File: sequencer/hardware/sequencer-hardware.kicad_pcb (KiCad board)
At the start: 4 copper layers, 100.6 x 151.4 mm, 116 parts, among them J1 Barrel Jack, J10 JST_4-pin_male, J11 Conn_01x03, J12 Conn_01x03, J13 Conn_01x03, J14 Conn_01x03, J15 JST_4-pin_male, J16 JST_4-pin_male, J17 Conn_01x03, J2 40Pin 0.1"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

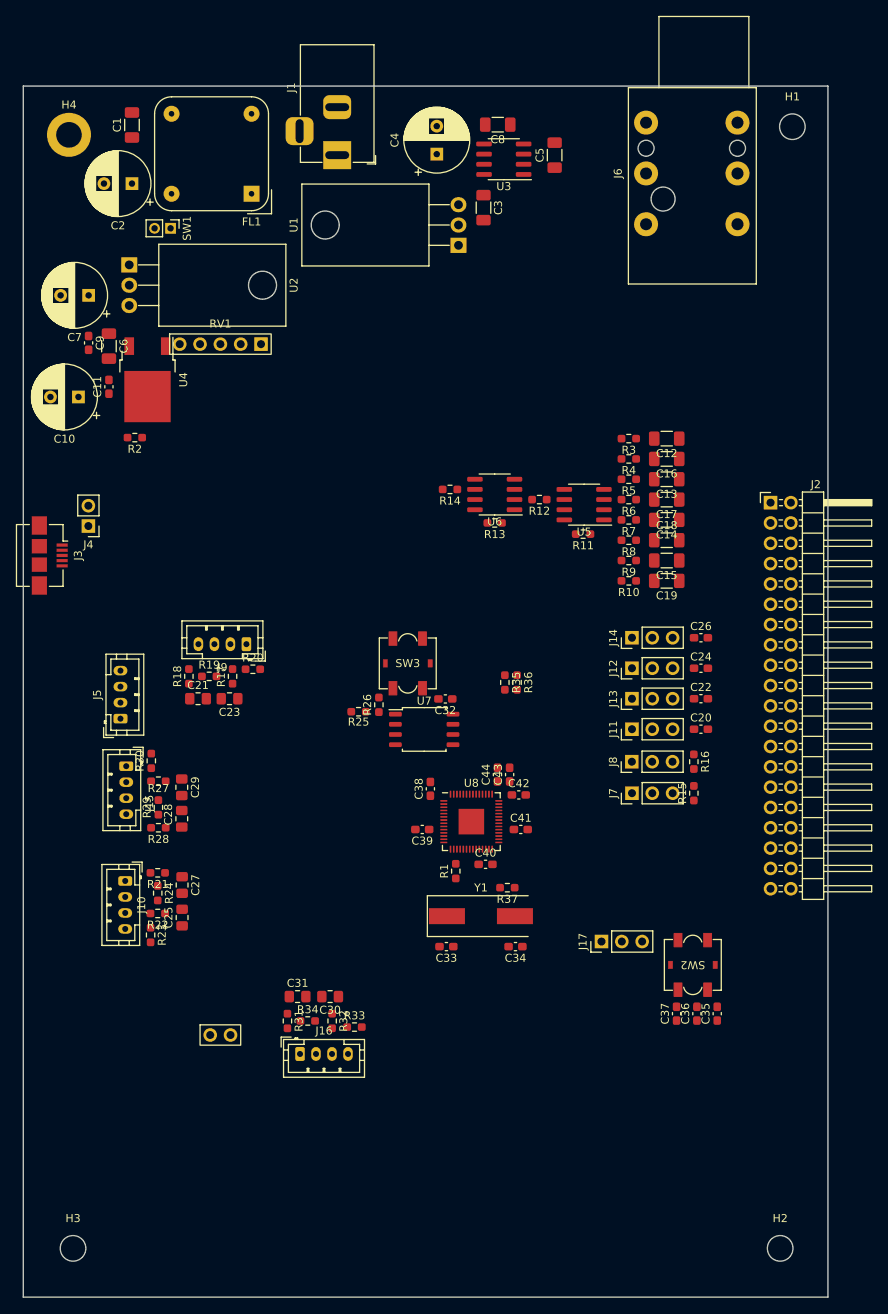
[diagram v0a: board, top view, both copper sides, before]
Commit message: Add ground planes
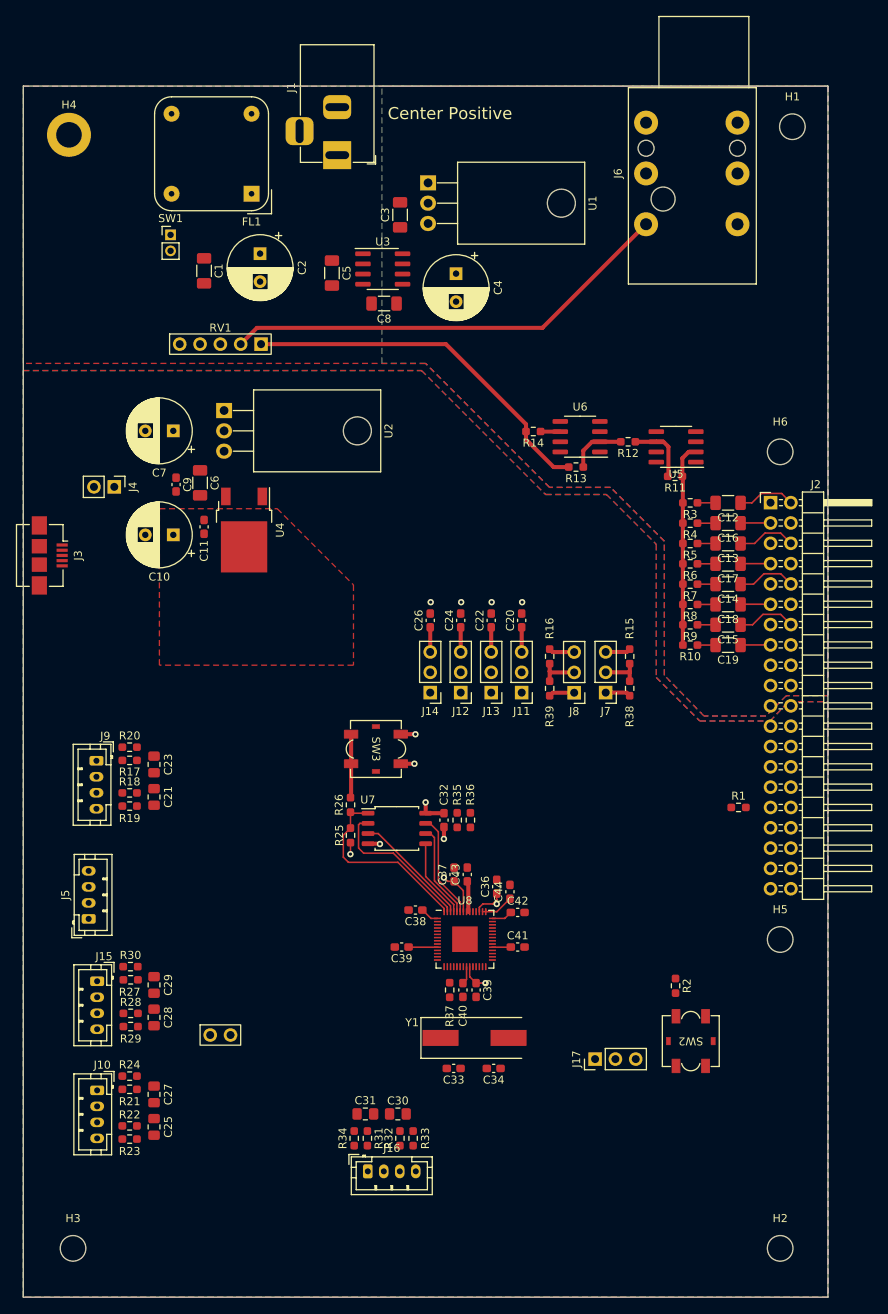
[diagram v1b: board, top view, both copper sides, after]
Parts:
- added H5: MountingHole, MountingHole:MountingHole_3.2mm_M3_ISO14580, F.Cu at (120.0, 132.1)
- added H6: MountingHole, MountingHole:MountingHole_3.2mm_M3_ISO14580, F.Cu at (120.0, 71.1)
- added R38: 10k, Resistor_SMD:R_0603_1608Metric_Pad0.98x0.95mm_HandSolder, F.Cu at (101.2, 100.7)
- added R39: 10k, Resistor_SMD:R_0603_1608Metric_Pad0.98x0.95mm_HandSolder, F.Cu at (91.2, 100.7)
- moved R2 96.2 mm to (106.9, 137.9), turned to -90 degrees
- moved R1 36.2 mm to (114.8, 115.6), turned to 0 degrees
- moved C26 33.9 mm to (76.3, 92.2), turned to 90 degrees
- moved C37 32.8 mm to (79.2, 124.0)
- moved C5 31.5 mm to (64.0, 48.8), turned to -90 degrees
- moved C24 30.6 mm to (80.1, 92.2), turned to 90 degrees
- moved C35 30.3 mm to (82.0, 138.4), turned to -90 degrees
- moved C36 29.6 mm to (84.6, 125.5)
- moved C22 28.0 mm to (83.9, 92.2), turned to 90 degrees
- moved R29 27.6 mm to (38.8, 143.0), turned to 0 degrees
- moved R21 27.3 mm to (38.7, 150.8)
- moved J15 27.1 mm to (34.6, 137.3)
- moved R22 26.8 mm to (38.7, 155.4)
- moved C8 26.5 mm to (70.5, 52.6), turned to 0 degrees
- moved C27 26.4 mm to (41.7, 151.4)
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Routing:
- net Net-(J6-PadT): track 0.00 -> 56.9 mm
- net Net-(R13-Pad2): track 0.00 -> 45.9 mm
- net +3V3: track 0.00 -> 45.2 mm, vias 0 -> 2
- net Net-(R10-Pad2): track 0.00 -> 25.4 mm
- net /D.R.U.M. Sequencer Digital/FCSB: track 0.00 -> 23.9 mm
- net /D.R.U.M. Sequencer Digital/FD1: track 0.00 -> 18.9 mm
- net /D.R.U.M. Sequencer Digital/FD2: track 0.00 -> 14.8 mm
- net +1V1: track 0.00 -> 14.2 mm, vias 0 -> 3
- net /D.R.U.M. Sequencer Digital/FD3: track 0.00 -> 13.1 mm
- net GNDD: track 0.00 -> 12.9 mm, vias 0 -> 8
- net /D.R.U.M. Sequencer Digital/FSCLK: track 0.00 -> 11.7 mm
- net /D.R.U.M. Sequencer Digital/FD0: track 0.00 -> 9.95 mm
- net Net-(R11-Pad2): track 0.00 -> 8.13 mm
- net Net-(R26-Pad2): track 0.00 -> 7.95 mm
- net /A7: track 0.00 -> 7.35 mm
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- added copper zone on In2.Cu, net +1V1
- added copper zone on B.Cu, net +3V3
- added copper zone on F.Cu, net +3V3
- added copper zone on B.Cu, net +5VA
- added copper zone on In2.Cu, net +5VD
- added copper zone on F.Cu, net GNDA
- added copper zone on In1.Cu, net GNDA
- added copper zone on F.Cu, net GNDD
- added copper zone on In1.Cu, net GNDD
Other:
- board text added: "Center Positive"

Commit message: Route analog domain
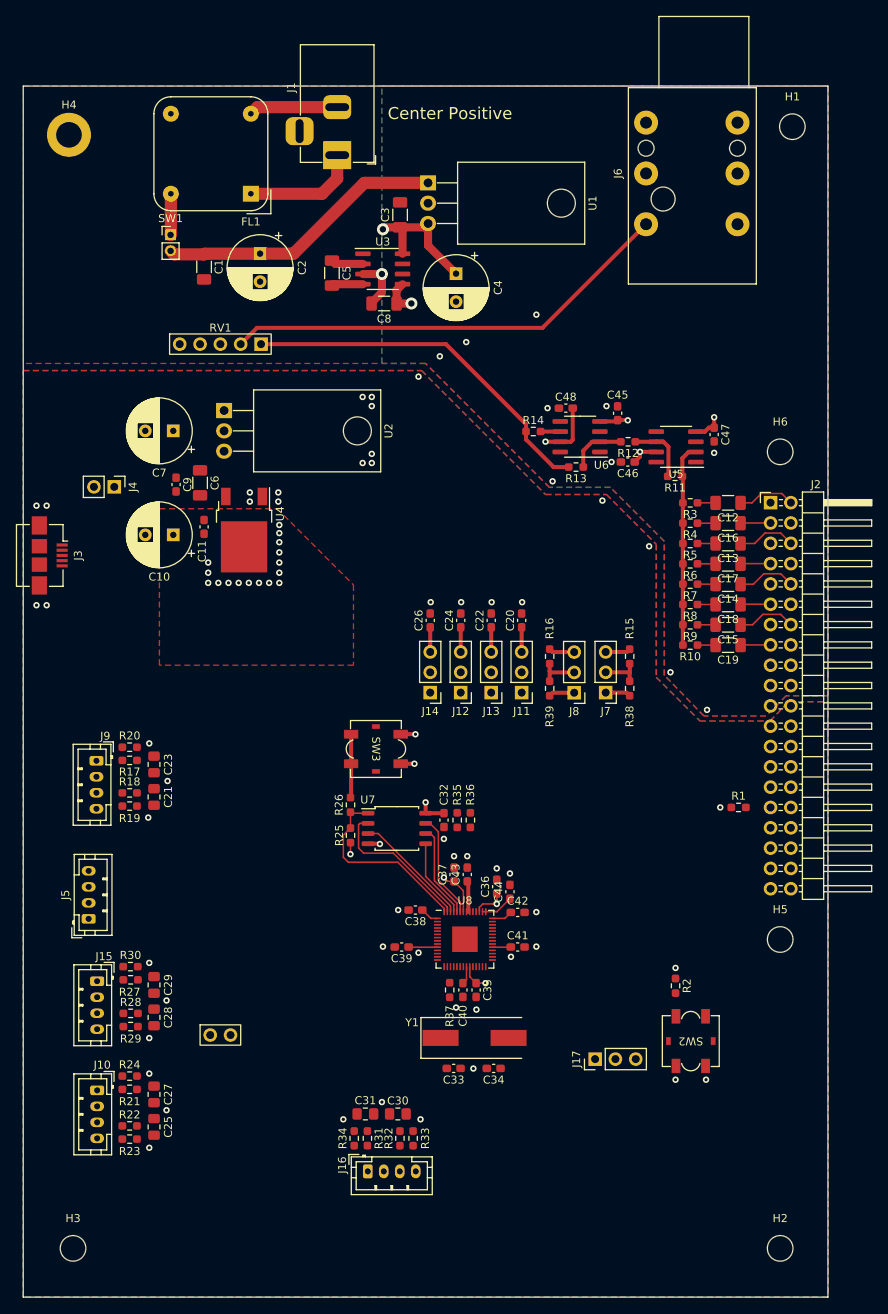
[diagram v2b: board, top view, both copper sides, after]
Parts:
- added C45: 1u, Capacitor_SMD:C_0603_1608Metric_Pad1.08x0.95mm_HandSolder, F.Cu at (99.7, 66.3)
- added C46: 1u, Capacitor_SMD:C_0603_1608Metric_Pad1.08x0.95mm_HandSolder, F.Cu at (101.0, 72.4)
- added C47: 1u, Capacitor_SMD:C_0603_1608Metric_Pad1.08x0.95mm_HandSolder, F.Cu at (111.8, 69.0)
- added C48: 1u, Capacitor_SMD:C_0603_1608Metric_Pad1.08x0.95mm_HandSolder, F.Cu at (93.2, 65.7)
- moved C1 0.49 mm to (48.0, 48.0)
- moved FL1 0.09 mm to (53.8, 38.9)
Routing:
- net -5V: track 0.00 -> 53.2 mm, vias 0 -> 3
- net +9V: track 0.00 -> 36.1 mm
- net +5VA: track 0.00 -> 24.4 mm, vias 0 -> 3
- net Net-(FL1-Pad1): track 0.00 -> 14.5 mm
- net Net-(FL1-Pad3): track 0.00 -> 11.1 mm
- net GNDA: track 0.00 -> 6.60 mm, vias 0 -> 11
- net Net-(FL1-Pad2): track 0.00 -> 5.15 mm
- net Net-(C5-Pad1): track 0.00 -> 4.05 mm
- net Net-(C5-Pad2): track 0.00 -> 3.94 mm
- net GNDD: track 12.9 -> 11.4 mm, vias 8 -> 42
- net +3V3: vias 2 -> 30

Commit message: Route digital domain
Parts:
- moved C35 0.93 mm to (82.0, 139.3)
- moved C40 0.55 mm to (80.4, 138.9)
- moved R37 0.55 mm to (78.7, 138.9)
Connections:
- U8 pad 12: /D.R.U.M. Sequencer Digital/GPIO9_ENC20 -> unconnected-(U8-Pad12)
- U8 pad 13: /D.R.U.M. Sequencer Digital/GPIO10_ENC21 -> /D.R.U.M. Sequencer Digital/GPIO9_ENC20
- U8 pad 14: unconnected-(U8-Pad14) -> /D.R.U.M. Sequencer Digital/GPIO10_ENC21
- U8 pad 18: /CBUS_NEXTPRSNT -> unconnected-(U8-Pad18)
- U8 pad 34: unconnected-(U8-Pad34) -> /CBUS_NEXTPRSNT
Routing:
- net /USB_D-: track 0.00 -> 71.9 mm
- net /USB_D+: track 0.00 -> 71.2 mm
- net /CBUS_SDRETIN: track 0.00 -> 48.2 mm, vias 0 -> 2
- net /D.R.U.M. Sequencer Digital/GPIO10_ENC21: track 0.00 -> 47.5 mm
- net /D.R.U.M. Sequencer Digital/GPIO1_ENC00: track 0.00 -> 46.5 mm
- net /CBUS_NEXTPRSNT: track 0.00 -> 45.4 mm
- net /KEY_SDA: track 0.00 -> 45.2 mm
- net /D.R.U.M. Sequencer Digital/GPIO26_ADC0: track 0.00 -> 45.2 mm
- net /D.R.U.M. Sequencer Digital/GPIO4_BTN0: track 5.21 -> 49.9 mm
- net /CBUS_SCK: track 0.00 -> 44.6 mm
- net /KEY_SCL: track 0.00 -> 44.6 mm
- net /D.R.U.M. Sequencer Digital/GPIO2_ENC01: track 0.00 -> 44.6 mm
- net /D.R.U.M. Sequencer Digital/GPIO27_ADC1: track 0.00 -> 44.4 mm
- net /D.R.U.M. Sequencer Digital/GPIO9_ENC20: track 0.00 -> 44.4 mm
- net /CBUS_EXTRA: track 0.00 -> 44.3 mm
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
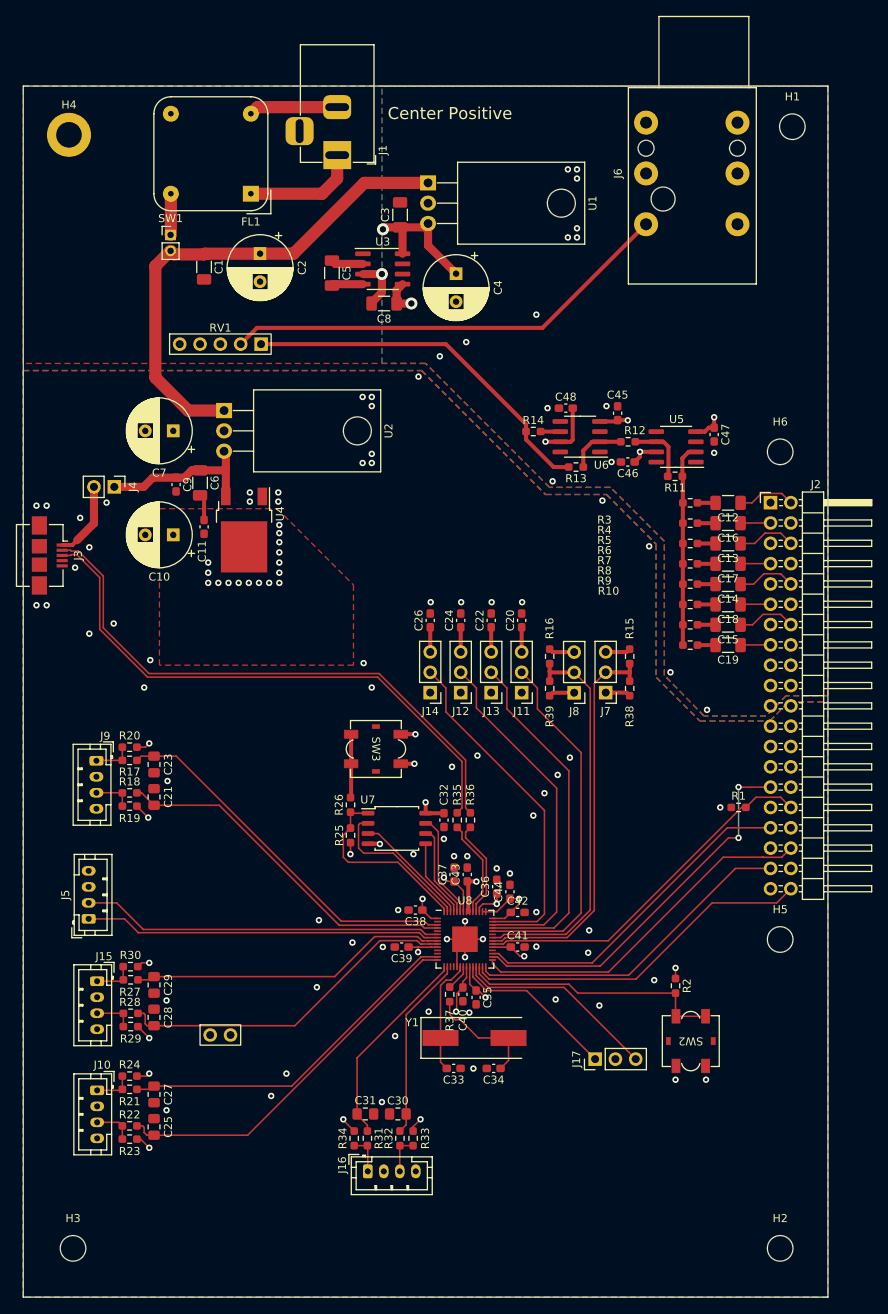
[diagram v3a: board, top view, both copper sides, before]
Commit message: Cleanup silkscreen
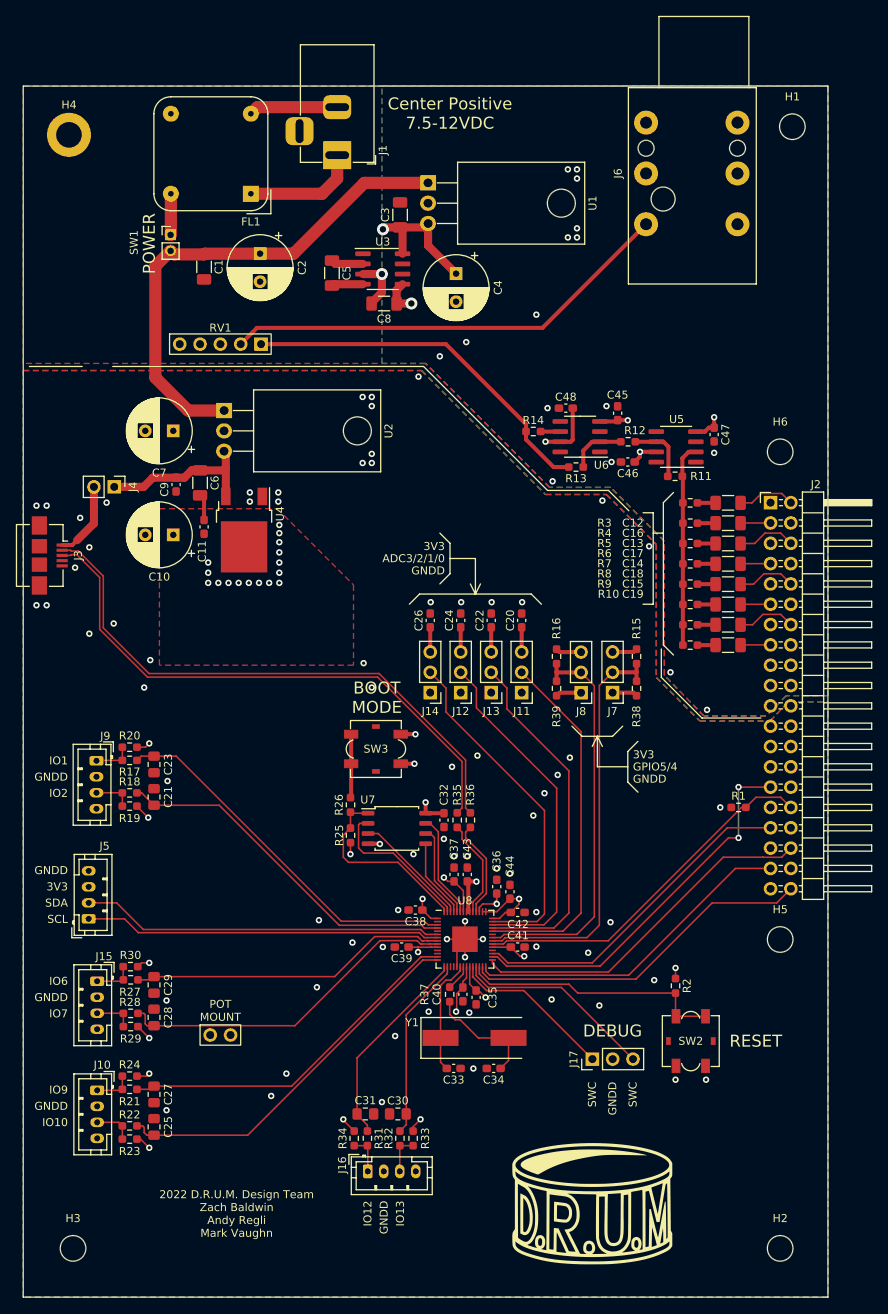
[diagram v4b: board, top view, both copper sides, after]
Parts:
- added G***: LOGO, LOGO, F.Cu at (96.5, 165.1)
- C2: value 100uF -> 220uF
- moved J7 0.86 mm to (99.1, 101.2)
- moved J8 0.86 mm to (95.1, 101.2)
- moved R15 0.86 mm to (102.1, 96.7)
- moved R16 0.86 mm to (92.1, 96.7)
- moved R38 0.86 mm to (102.1, 100.7)
- moved R39 0.86 mm to (92.1, 100.7)
- moved J17 0.34 mm to (96.5, 147.0)
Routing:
- net /D.R.U.M. Sequencer Digital/GPIO4_BTN0: track 49.9 -> 51.7 mm
- net /D.R.U.M. Sequencer Digital/GPIO5_BTN1: track 49.5 -> 50.3 mm
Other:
- board text added: "2022 D.R.U.M. Design Team Zach Baldwin Andy Regli Mark Vaughn"
- board text added: "3V3"
- board text added: "ADC3/2/1/0"
- board text added: "BOOT MODE"
- board text added: "Center Positive 7.5-12VDC"
- board text added: "D.R.U.M. - Module HW Design REV: 1.0 Layout REV: A Order No. P/N DRUM-DM-1001"
- board text added: "DEBUG"
- board text added: "GNDD"
- board text added: "GPIO5/4"
- board text added: "IO1"
- board text added: "IO10"
- board text added: "IO12"
- board text added: "IO13"
- board text added: "IO2"
- board text added: "IO6"
- board text added: "IO7"
- board text added: "IO9"
- board text added: "POT MOUNT"
- board text added: "POWER"
- board text added: "RESET"
- board text added: "SCL"
- board text added: "SDA"
- board text added: "SWC"
- board text removed: "Center Positive"
